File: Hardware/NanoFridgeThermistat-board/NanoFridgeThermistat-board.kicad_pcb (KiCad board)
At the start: 2 copper layers, 68.6 x 48.3 mm, 18 parts, among them J1 Connector_Thermistor, J2 Main_Connector, J3 CompressorMotor_Connector, J4 I2C_Conn, U1 MOC3042M

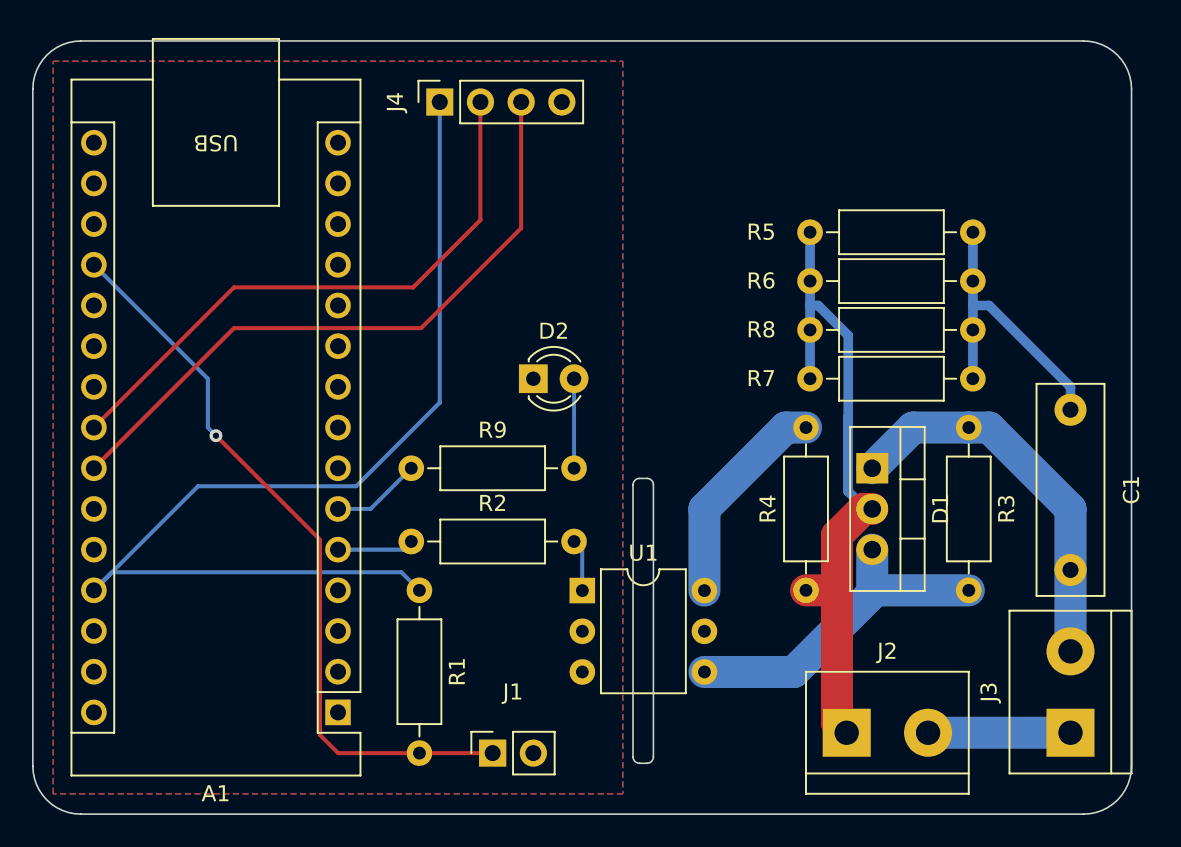
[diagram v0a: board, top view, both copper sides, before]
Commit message: Improved routing for hardware
Signed-off-by: bebenlebricolo <benoittarrade@hotmail.fr>
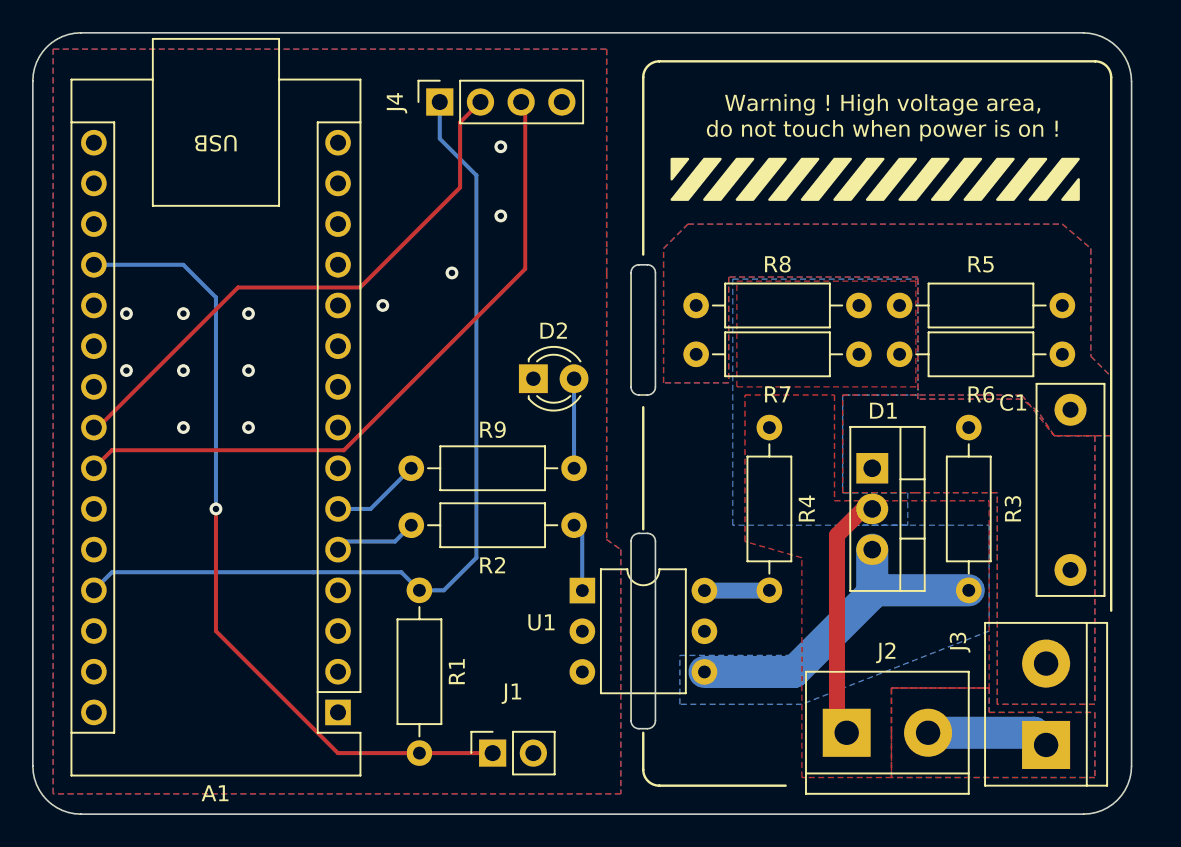
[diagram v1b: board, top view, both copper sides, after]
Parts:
- moved R7 17.3 mm to (121.4, 79.2), turned to 0 degrees
- moved R8 17.3 mm to (121.4, 76.2), turned to 0 degrees
- moved R4 10.4 mm to (126.0, 83.8), turned to -90 degrees
- moved R5 7.22 mm to (144.3, 76.2)
- moved R6 7.22 mm to (144.3, 79.2)
- moved J3 1.70 mm to (143.3, 103.6)
- moved R2 1.02 mm to (103.6, 89.9)
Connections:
- net Net-(C1-Pad1) renamed /SnubberResLow
- net Net-(D1-A1) renamed /NeutralTriac
- net Net-(D1-G) renamed /Trigger
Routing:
- net Main_HOT: track 46.0 -> 15.5 mm
- net /NeutralTriac: track 24.4 -> 0.00 mm
- net /SnubberResLow: track 18.8 -> 0.00 mm
- net Vcc: track 66.5 -> 55.0 mm
- net Net-(R4-Pad2): track 13.5 -> 4.06 mm
- net Temp: track 46.4 -> 49.7 mm
- net SDA: track 36.9 -> 34.9 mm
- net SCL: track 40.8 -> 42.6 mm
- net Main_Neutral: track 8.89 -> 7.68 mm
- net Net-(R2-Pad2): track 3.28 -> 4.29 mm
- net GND: vias 0 -> 12
- added copper zone on B.Cu, net /NeutralTriac
- added copper zone on F.Cu, net /NeutralTriac
- added copper zone on B.Cu, net /SnubberResLow
- added copper zone on F.Cu, net /SnubberResLow
- added copper zone on B.Cu, net /Trigger
- added copper zone on F.Cu, net GND
- added copper zone on B.Cu, net Main_HOT
- added copper zone on F.Cu, net Main_HOT
- added copper zone on B.Cu, net Main_Neutral
- added copper zone on F.Cu, net Main_Neutral
- removed copper zone on F.Cu, net (none)
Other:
- board size 68.6 x 48.3 mm -> 68.6 x 48.8 mm
- board text added: "Warning ! High voltage area, do not touch when power is on !"

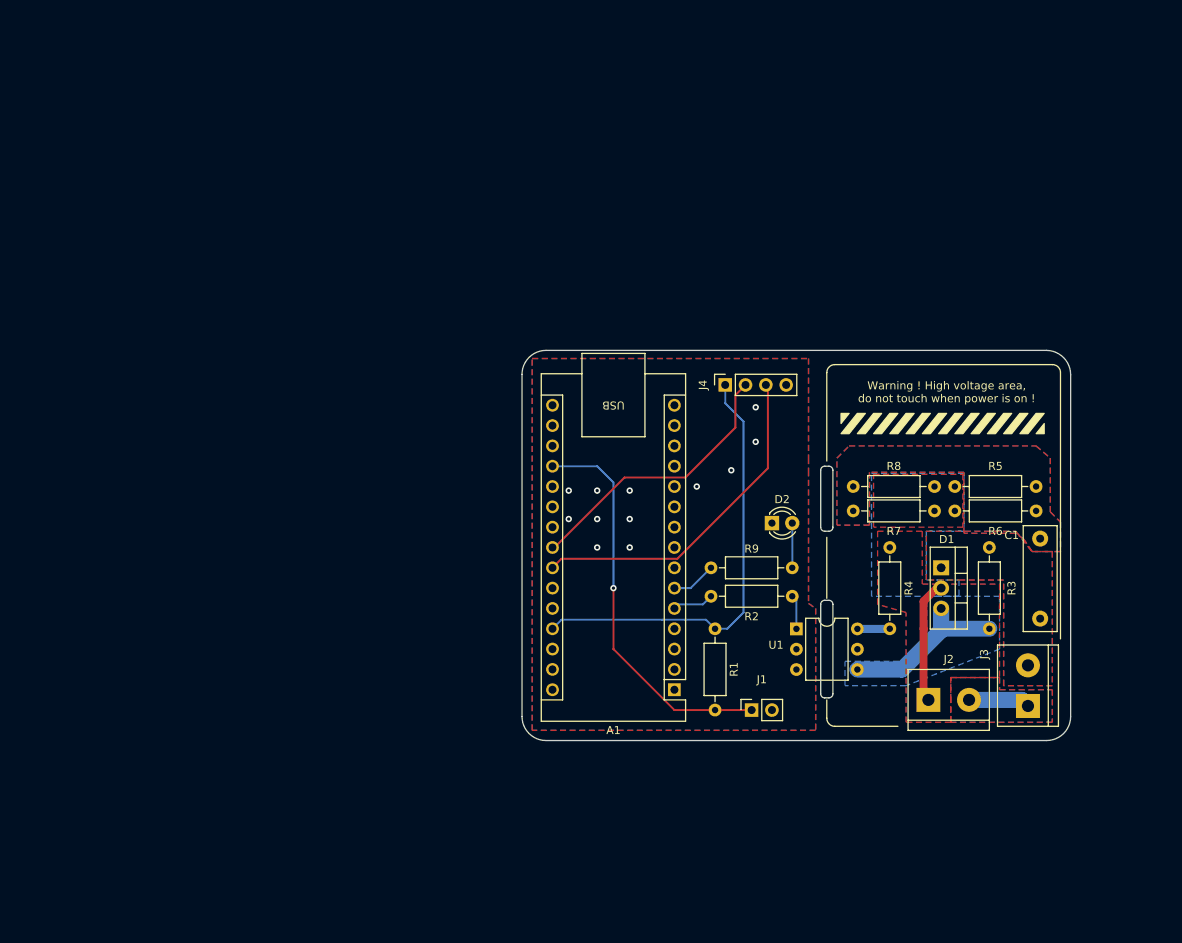
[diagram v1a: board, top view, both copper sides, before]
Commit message: Added more parts sourcing
Signed-off-by: bebenlebricolo <benoittarrade@hotmail.fr>
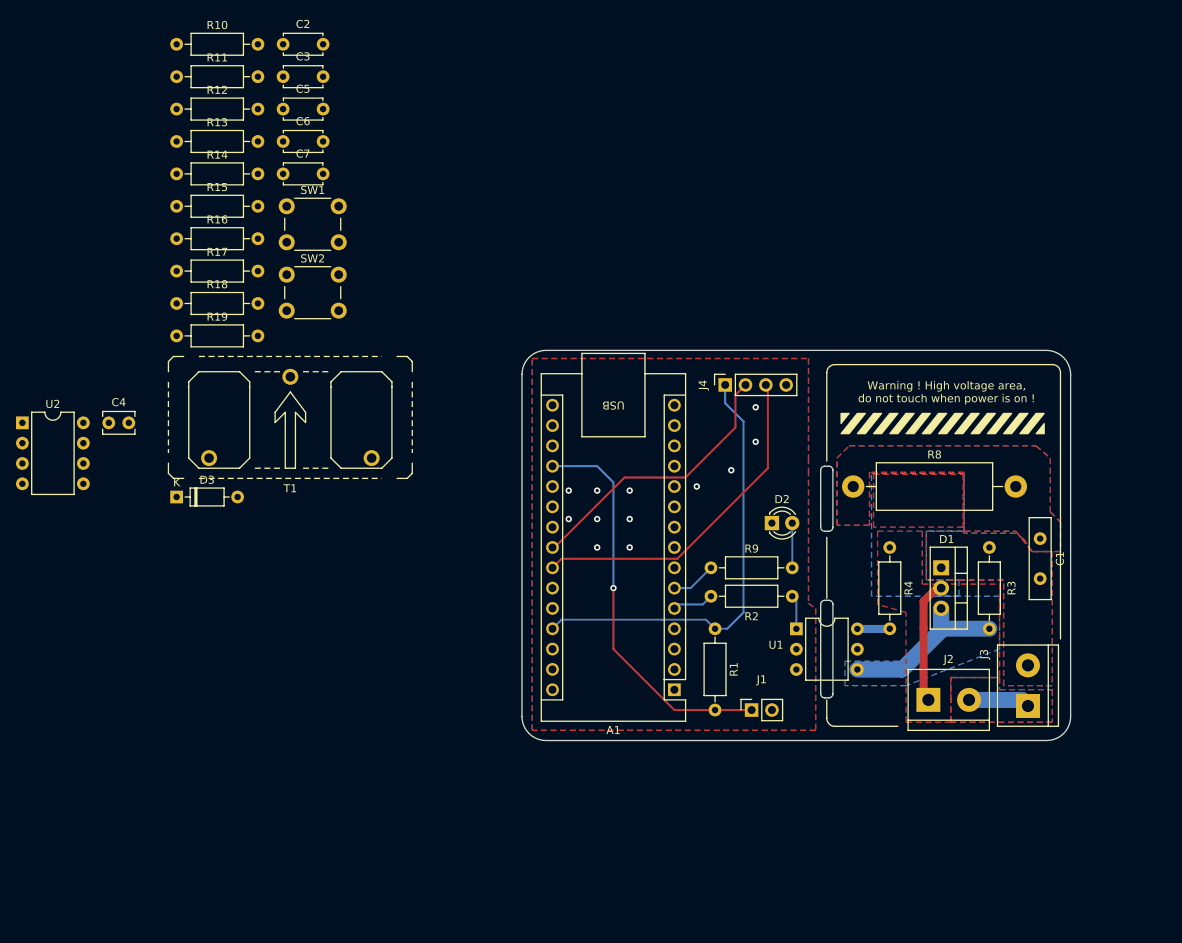
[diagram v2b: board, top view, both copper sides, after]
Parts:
- removed R5, R6, R7: 1.2k, Resistor_THT:R_Axial_DIN0207_L6.3mm_D2.5mm_P10.16mm_Horizontal
- added C2: 1u, Capacitor_THT:C_Disc_D4.7mm_W2.5mm_P5.00mm, F.Cu at (50.1, 20.9)
- added C3: 1u, Capacitor_THT:C_Disc_D4.7mm_W2.5mm_P5.00mm, F.Cu at (50.1, 25.0)
- added C4: 100n, Capacitor_THT:C_Disc_D3.8mm_W2.6mm_P2.50mm, F.Cu at (28.4, 68.2)
- added C5: 1u, Capacitor_THT:C_Disc_D4.7mm_W2.5mm_P5.00mm, F.Cu at (50.1, 29.0)
- added C6: 1u, Capacitor_THT:C_Disc_D4.7mm_W2.5mm_P5.00mm, F.Cu at (50.1, 33.1)
- added C7: 1u, Capacitor_THT:C_Disc_D4.7mm_W2.5mm_P5.00mm, F.Cu at (50.1, 37.1)
- added D3: D_Zener, Diode_THT:D_DO-35_SOD27_P7.62mm_Horizontal, F.Cu at (36.8, 77.5)
- added R10: 1k, Resistor_THT:R_Axial_DIN0207_L6.3mm_D2.5mm_P10.16mm_Horizontal, F.Cu at (36.8, 20.9)
- added R11: 1k, Resistor_THT:R_Axial_DIN0207_L6.3mm_D2.5mm_P10.16mm_Horizontal, F.Cu at (36.8, 25.0)
- added R12: 22k, Resistor_THT:R_Axial_DIN0207_L6.3mm_D2.5mm_P10.16mm_Horizontal, F.Cu at (36.8, 29.0)
- added R13: 100 / 0,25W, Resistor_THT:R_Axial_DIN0207_L6.3mm_D2.5mm_P10.16mm_Horizontal, F.Cu at (36.8, 33.1)
- added R14: 2.2k, Resistor_THT:R_Axial_DIN0207_L6.3mm_D2.5mm_P10.16mm_Horizontal, F.Cu at (36.8, 37.1)
- added R15: 100k, Resistor_THT:R_Axial_DIN0207_L6.3mm_D2.5mm_P10.16mm_Horizontal, F.Cu at (36.8, 41.2)
- added R16: 10k, Resistor_THT:R_Axial_DIN0207_L6.3mm_D2.5mm_P10.16mm_Horizontal, F.Cu at (36.8, 45.2)
- added R17: 100k, Resistor_THT:R_Axial_DIN0207_L6.3mm_D2.5mm_P10.16mm_Horizontal, F.Cu at (36.8, 49.3)
- added R18: 100k, Resistor_THT:R_Axial_DIN0207_L6.3mm_D2.5mm_P10.16mm_Horizontal, F.Cu at (36.8, 53.3)
- added R19: 100k, Resistor_THT:R_Axial_DIN0207_L6.3mm_D2.5mm_P10.16mm_Horizontal, F.Cu at (36.8, 57.4)
- added SW1: SW_Push, Button_Switch_THT:SW_PUSH_6mm, F.Cu at (50.6, 41.2)
- added SW2: SW_Push, Button_Switch_THT:SW_PUSH_6mm, F.Cu at (50.6, 49.7)
- added T1: CST1, CurrentTransformer:CT-RSPRO-1243888, F.Cu at (51.1, 72.6)
- added U2: TL072, Package_DIP:DIP-8_W7.62mm, F.Cu at (17.6, 68.2)
- A1: value Arduino_Nano_Every -> Arduino_Nano_v3.x
- C1: value 10n -> 10n / 500V+ AC; footprint Capacitor_THT:C_Rect_L13.0mm_W4.0mm_P10.00mm_FKS3_FKP3_MKS4 -> Capacitor_THT:C_Disc_D10.0mm_W2.5mm_P5.00mm
- R8: value 1.2k -> 330Ω / 1W; footprint Resistor_THT:R_Axial_DIN0207_L6.3mm_D2.5mm_P10.16mm_Horizontal -> Resistor_THT:R_Axial_DIN0614_L14.3mm_D5.7mm_P20.32mm_Horizontal
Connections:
- A1 pad 20: unconnected-(A1-A1-Pad20) -> CurrentSense
- A1 pad 30: unconnected-(A1-VIN-Pad30) -> Vcc
- A1 pad 7: unconnected-(A1-D4-Pad7) -> +Button
- A1 pad 8: unconnected-(A1-D5-Pad8) -> -Button

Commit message: Upgraded board with new models, components and layout
Signed-off-by: bebenlebricolo <benoittarrade@hotmail.fr>
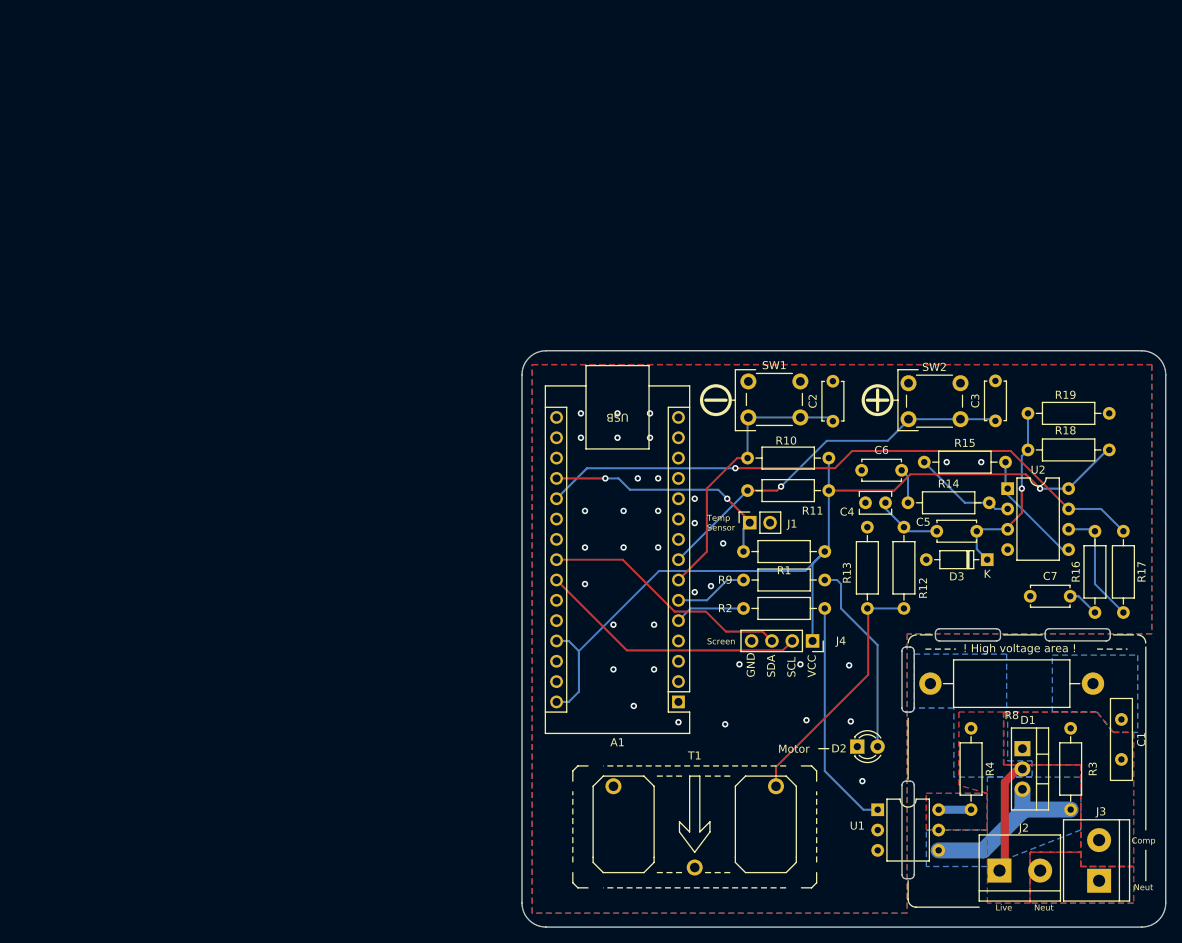
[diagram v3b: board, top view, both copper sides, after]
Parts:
- J2, J3: footprint TerminalBlock:TerminalBlock_bornier-2_P5.08mm -> TEConnectors:TE-282836-2-5.08mm
- moved R17 125.8 mm to (155.2, 91.9), turned to 90 degrees
- moved R16 123.9 mm to (151.6, 91.9), turned to 90 degrees
- moved U2 123.4 mm to (140.7, 76.5)
- moved R19 117.0 mm to (153.4, 67.1), turned to 180 degrees
- moved R12 110.3 mm to (127.8, 91.4), turned to 90 degrees
- moved R18 108.0 mm to (143.3, 71.6)
- moved C7 107.3 mm to (143.5, 89.9)
- moved D3 101.6 mm to (138.2, 85.3), turned to 180 degrees
- moved R14 100.2 mm to (128.3, 78.2)
- moved C3 98.9 mm to (139.2, 68.0), turned to 90 degrees
- moved R13 98.9 mm to (123.2, 81.3), turned to -90 degrees
- moved R15 98.8 mm to (130.3, 73.2)
- moved C4 97.6 mm to (125.4, 78.2), turned to 180 degrees
- moved C5 97.3 mm to (131.9, 81.8)
- moved R11 96.6 mm to (118.4, 76.7), turned to 180 degrees
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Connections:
- net Net-(R4-Pad2) renamed /TriacDriverAC1
- J4 pad 2: SDA -> SCL
- J4 pad 3: SCL -> SDA
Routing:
- net CurrentSense: track 0.00 -> 77.5 mm, vias 0 -> 1
- net Vcc: track 55.0 -> 112.8 mm, vias 0 -> 1
- net -Button: track 0.00 -> 47.1 mm, vias 0 -> 1
- net +Button: track 0.00 -> 35.4 mm
- net Net-(T1-A): track 0.00 -> 31.6 mm
- net Net-(R2-Pad2): track 4.29 -> 28.9 mm
- net Polarisation: track 0.00 -> 23.6 mm, vias 0 -> 1
- net Temp: track 49.7 -> 30.5 mm, vias 1 -> 2
- net Net-(D2-A): track 5.59 -> 24.5 mm
- net Net-(U2B--): track 0.00 -> 15.0 mm
- net Net-(U2B-+): track 0.00 -> 14.6 mm
- net Net-(U2A--): track 0.00 -> 12.8 mm
- net SCL: track 42.6 -> 33.6 mm
- net Net-(C4-Pad1): track 0.00 -> 8.32 mm
- net Main_Neutral: track 7.68 -> 0.00 mm
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- added copper zone on B.Cu, net /TriacDriverAC1
- added copper zone on F.Cu, net /TriacDriverAC1
- removed copper zone on F.Cu, net /SnubberResLow
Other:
- board size 68.6 x 48.8 mm -> 80.5 x 72 mm
- board text added: "! High voltage area !"
- board text added: "Comp"
- board text added: "GND"
- board text added: "Live"
- board text added: "Motor"
- board text added: "Neut"
- board text added: "SCL"
- board text added: "SDA"
- board text added: "Screen"
- board text added: "Temp Sensor"
- board text added: "VCC"
